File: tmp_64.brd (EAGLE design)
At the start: 31.8 x 169.4 mm, 0 parts

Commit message: union signal
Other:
- board size 31.8 x 169.4 mm -> 31.8 x 168 mm
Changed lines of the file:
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@@
 <plain>
 <wire x1="0" y1="0" x2="31.78" y2="0" width="0" layer="20"/>
-<wire x1="31.78" y1="0" x2="31.78" y2="169.42" width="0" layer="20"/>
-<wire x1="31.78" y1="169.42" x2="0" y2="169.42" width="0" layer="20"/>
-<wire x1="0" y1="169.42" x2="0" y2="0" width="0" layer="20"/>
+<wire x1="31.78" y1="0" x2="31.78" y2="168.02" width="0" layer="20"/>
+<wire x1="31.78" y1="168.02" x2="0" y2="168.02" width="0" layer="20"/>
+<wire x1="0" y1="168.02" x2="0" y2="0" width="0" layer="20"/>
 </plain>
 <attributes>
@@
 </class>
 </classes>
-<designrules name="default">
+<designrules name="default *">
 <description language="de">&lt;b&gt;EAGLE Design Rules&lt;/b&gt;
 &lt;p&gt;
@@
 <param name="mtCopper" value="0.035mm 0.035mm 0.035mm 0.035mm 0.035mm 0.035mm 0.035mm 0.035mm 0.035mm 0.035mm 0.035mm 0.035mm 0.035mm 0.035mm 0.035mm 0.035mm"/>
 <param name="mtIsolate" value="1.5mm 0.15mm 0.2mm 0.15mm 0.2mm 0.15mm 0.2mm 0.15mm 0.2mm 0.15mm 0.2mm 0.15mm 0.2mm 0.15mm 0.2mm"/>
-<param name="mdWireWire" value="8mil"/>
-<param name="mdWirePad" value="8mil"/>
+<param name="mdWireWire" value="12mil"/>
+<param name="mdWirePad" value="10mil"/>
 <param name="mdWireVia" value="8mil"/>
 <param name="mdPadPad" value="8mil"/>

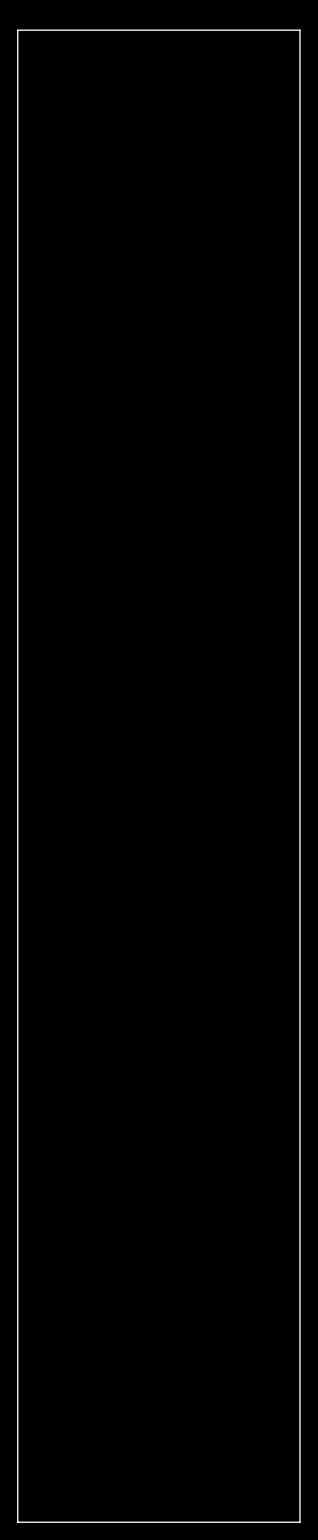
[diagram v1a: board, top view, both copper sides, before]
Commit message: modified display
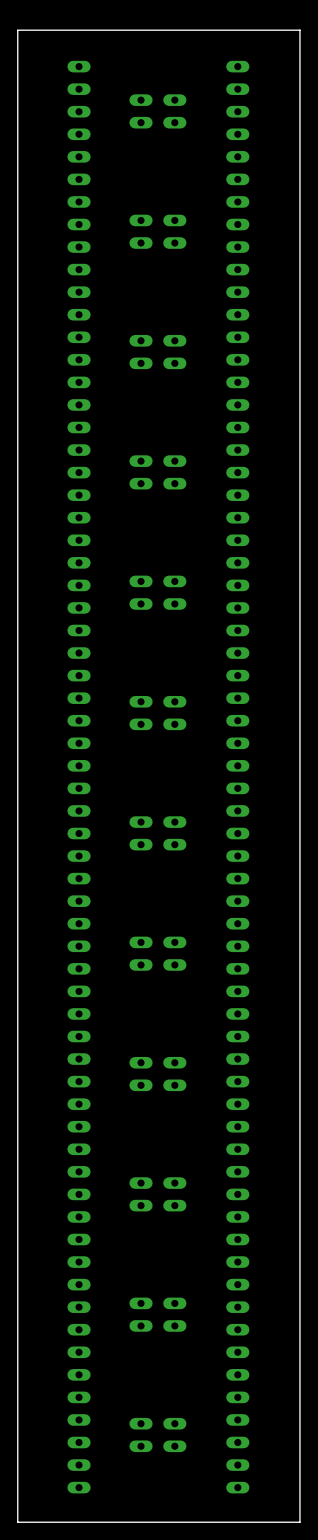
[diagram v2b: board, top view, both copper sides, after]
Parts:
- added LL0, LL1, LL10, LL11, LL12, LL13, LL14, LL15, LL16, LL17, LL18, LL19, LL2, LL20, LL21, LL22, LL23, LL24, LL25, LL26, LL27, LL28, LL29, LL3, LL30, LL31, LL32, LL33, LL34, LL35, LL36, LL37, LL38, LL39, LL4, LL40, LL41, LL42, LL43, LL44, LL45, LL46, LL47, LL48, LL49, LL5, LL50, LL51, LL52, LL53, LL54, LL55, LL56, LL57, LL58, LL59, LL6, LL60, LL61, LL62, LL63, LL7, LL8, LL9, LS0, LS1, LS10, LS11, LS12, LS13, LS14, LS15, LS16, LS17, LS18, LS19, LS2, LS20, LS21, LS22, LS23, LS3, LS4, LS5, LS6, LS7, LS8, LS9, RL0, RL1, RL10, RL11, RL12, RL13, RL14, RL15, RL16, RL17, RL18, RL19, RL2, RL20, RL21, RL22, RL23, RL24, RL25, RL26, RL27, RL28, RL29, RL3, RL30, RL31, RL32, RL33, RL34, RL35, RL36, RL37, RL38, RL39, RL4, RL40, RL41, RL42, RL43, RL44, RL45, RL46, RL47, RL48, RL49, RL5, RL50, RL51, RL52, RL53, RL54, RL55, RL56, RL57, RL58, RL59, RL6, RL60, RL61, RL62, RL63, RL7, RL8, RL9, RS0, RS1, RS10, RS11, RS12, RS13, RS14, RS15, RS16, RS17, RS18, RS19, RS2, RS20, RS21, RS22, RS23, RS3, RS4, RS5, RS6, RS7, RS8, RS9: (no value), SparkFun-Connectors:1X01_OVAL_PIN_AUTO
